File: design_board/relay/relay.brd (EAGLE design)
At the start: 15 x 132.2 mm, 9 parts, among them K1 FRS1B

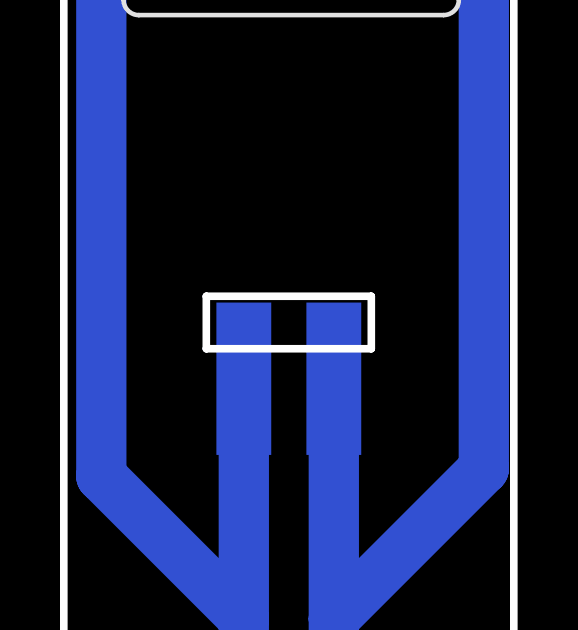
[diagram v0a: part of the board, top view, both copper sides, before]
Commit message: Изменены платы controller.brd и relay.brd - скорректированы зазоры между платами, оp_amp.brd - добавлено отверстие для прокладки проводки между уровнями. Изменена схема сontroller.sch - добавлены номиналы резисторов обвязки оптопар.
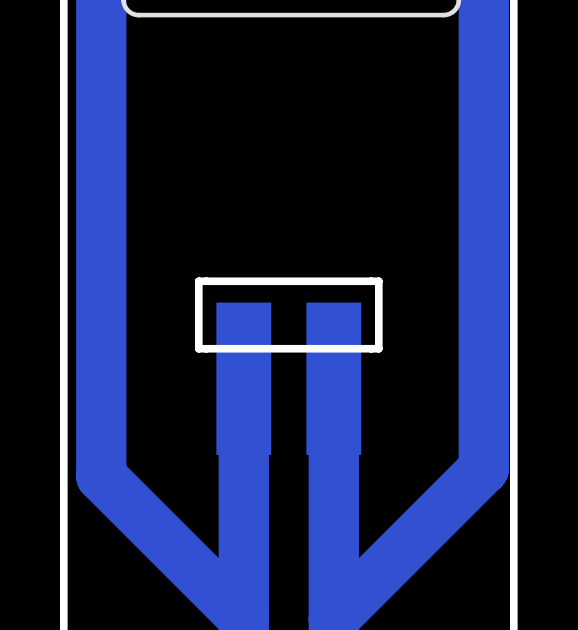
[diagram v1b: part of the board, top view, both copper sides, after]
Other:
- outline, holes or cut-outs redrawn
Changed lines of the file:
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@@
 <wire x1="26.75" y1="-41.75" x2="32.25" y2="-41.75" width="0.254" layer="20"/>
 <wire x1="26.75" y1="36.5" x2="32.25" y2="36.5" width="0.254" layer="20"/>
-<wire x1="26.75" y1="36.5" x2="26.75" y2="38.25" width="0.254" layer="20"/>
-<wire x1="32.25" y1="38.25" x2="32.25" y2="36.5" width="0.254" layer="20"/>
 <dimension x1="26.75" y1="-37.5" x2="26.75" y2="-2.5" x3="18.75" y3="-20" textsize="1.778" layer="19"/>
 <wire x1="26.75" y1="-37.5" x2="22" y2="-37.5" width="0.254" layer="20"/>
@@
 <dimension x1="26.75" y1="-41.75" x2="32.25" y2="-41.75" x3="29.5" y3="-43.25" textsize="1.778" layer="19"/>
 <dimension x1="26.75" y1="-41.75" x2="26.75" y2="-37.5" x3="16.75" y3="-39.625" textsize="1.778" layer="19"/>
-<wire x1="26.75" y1="38.25" x2="32.25" y2="38.25" width="0.254" layer="20"/>
+<dimension x1="26.75" y1="36.5" x2="26.75" y2="38.75" x3="39.75" y3="37.625" textsize="1.778" layer="19"/>
+<wire x1="26.75" y1="36.5" x2="26.5" y2="36.5" width="0.254" layer="20"/>
+<wire x1="26.5" y1="36.5" x2="26.5" y2="38.75" width="0.254" layer="20"/>
+<wire x1="26.5" y1="38.75" x2="26.75" y2="38.75" width="0.254" layer="20"/>
+<wire x1="26.75" y1="38.75" x2="32.25" y2="38.75" width="0.254" layer="20"/>
+<wire x1="32.25" y1="38.75" x2="32.5" y2="38.75" width="0.254" layer="20"/>
+<wire x1="32.5" y1="38.75" x2="32.5" y2="36.5" width="0.254" layer="20"/>
+<wire x1="32.5" y1="36.5" x2="32.25" y2="36.5" width="0.254" layer="20"/>
 </plain>
 <attributes>
